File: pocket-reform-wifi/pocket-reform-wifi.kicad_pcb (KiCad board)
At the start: 4 copper layers, 27.6 x 95 mm, 42 parts, among them J1 Bus_M.2_Socket_E, J2 Conn_01x20, J21 CONN_HEAD, J22 SJ-43516-SMT, J24 CONN_PWRSW, SW21 SW_DIP_x01, U1 TPS62A04ABDRL, X1 ECS-327MVATX-2-CN-TR3

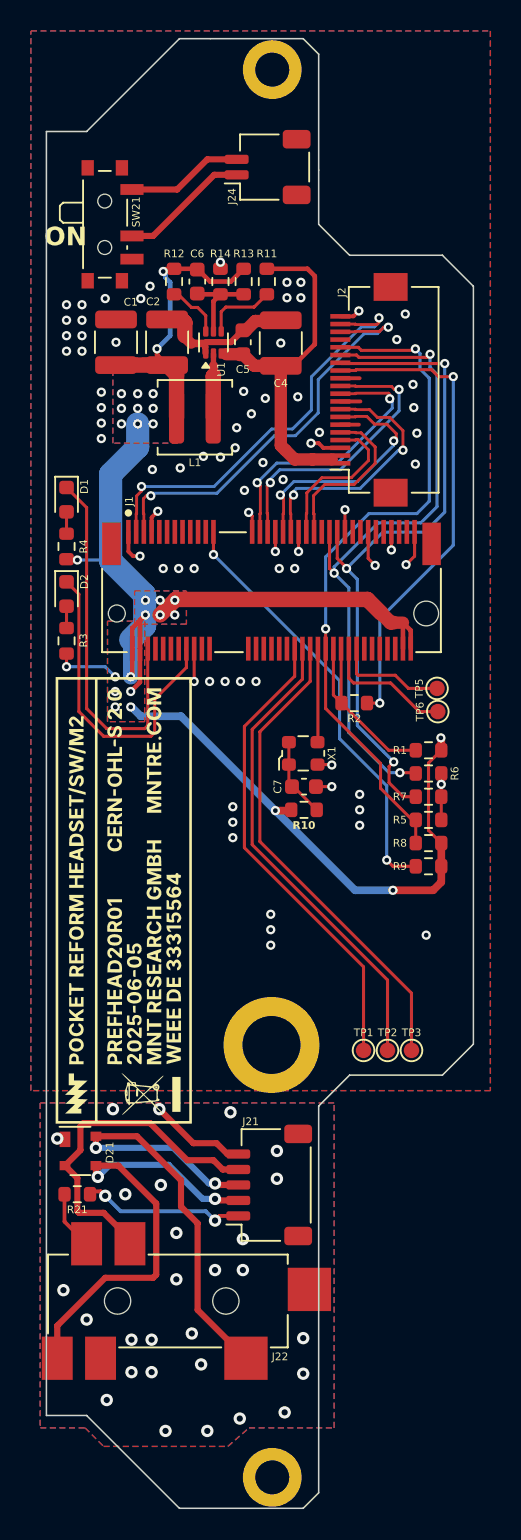
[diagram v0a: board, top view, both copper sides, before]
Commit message: pocket-reform-wifi: revision r2 with different inductor footprint
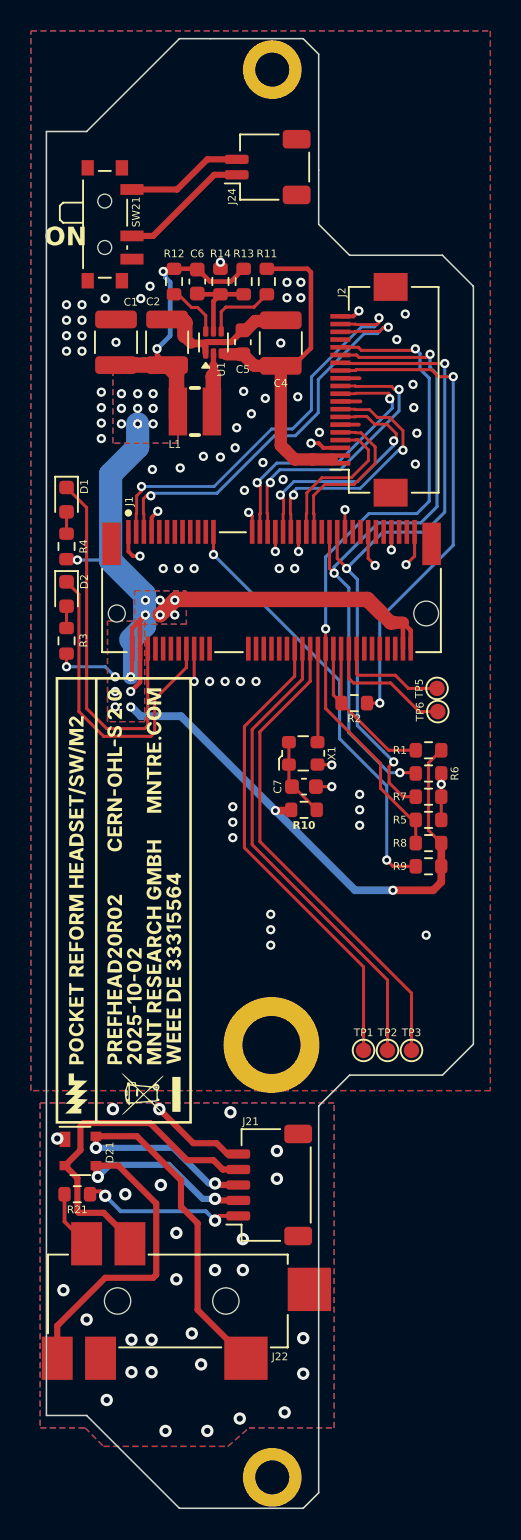
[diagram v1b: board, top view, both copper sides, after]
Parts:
- H1: footprint Mounting_Wuerth:Mounting_Wuerth_WA-SMSI-M2_H1.5mm_9774015243 -> footprints:Mounting_Sinhoo_SMTSO20
- L1: value 220nH XAL4020-221MEB -> 220nH 10A; footprint Inductor_SMD:L_Coilcraft_XAL4020-XXX -> EasyEDA:IND-SMD_L3.0-W3.0_FTC303020D
- moved L1 0.38 mm to (95.0, 101.1)
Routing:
- net +3V3: track 111.8 -> 111.0 mm, vias 28 -> 27

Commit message: pocket-reform-wifi: revision r2 part selection tweaks for new batch
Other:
- board text added: "JLCPCB Stackup JLC04101H-3313, 85 ohms diff impedance"
- board text removed: "JLCPCB Stackup JLC04081H-3313"
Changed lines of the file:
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@@
 			)
 		)
-		(property "Manufacturer_No" "2199119-4"
+		(property "Manufacturer_No" "2199230-4"
 			(at 0 0 0)
 			(unlocked yes)
@@
 			)
 		)
-		(property "Notes" ""
+		(property "Notes" "original was 2199119-4, 1mm less height. match with nut height!"
 			(at 0 0 0)
 			(unlocked yes)
@@
 			)
 		)
-		(property "Alt_Part_No" ""
+		(property "Alt_Part_No" "2199119-4 (with nut SMTSO2015CTJ)"
 			(at 0 0 0)
 			(unlocked yes)
@@
 			)
 		)
-		(property "LCSC" "global sourcing"
+		(property "LCSC" "C41447443"
 			(at 0 0 0)
 			(unlocked yes)
@@
 			)
 		)
-		(property "Manufacturer_No" "SMTSO2015CTJ"
+		(property "Manufacturer_No" "SMTSO2025CTJ"
 			(at 0 0 90)
 			(unlocked yes)
@@
 			)
 		)
-		(property "Notes" ""
+		(property "Notes" "match height with m.2 socket!"
 			(at 0 0 90)
 			(unlocked yes)
@@
 			)
 		)
-		(property "Alt_Manufacturer" "Wuerth"
+		(property "Alt_Manufacturer" ""
 			(at 0 0 90)
 			(unlocked yes)
@@
 			)
 		)
-		(property "Alt_Part_No" "9774015243"
+		(property "Alt_Part_No" "SMTSO2015CTJ for lower height m.2 socket"
 			(at 0 0 90)
 			(unlocked yes)
@@
 			)
 		)
-		(property "LCSC" "C2916320"
+		(property "LCSC" "C2916321"
 			(at 0 0 90)
 			(unlocked yes)
@@
 			)
 		)
-		(property "Manufacturer" "Vishay Dale"
+		(property "Manufacturer" "UNI-ROYAL"
 			(at 0 0 270)
 			(unlocked yes)
@@
 			)
 		)
-		(property "Manufacturer_No" "CRCW0603453KFKEA"
+		(property "Manufacturer_No" "0603WAF4533T5E"
 			(at 0 0 270)
 			(unlocked yes)
@@
 			)
 		)
-		(property "LCSC" "C2079749"
+		(property "LCSC" "C25818"
 			(at 0 0 270)
 			(unlocked yes)
@@
 			)
 		)
-		(property "Manufacturer" "ECS"
+		(property "Manufacturer" "SCTF"
 			(at 0 0 90)
 			(unlocked yes)
@@
 			)
 		)
-		(property "Manufacturer_No" "ECS-327MVATX-2-CN-TR3"
+		(property "Manufacturer_No" "SX2M32.768KM20F30TNN"
 			(at 0 0 90)
 			(unlocked yes)
@@
 			)
 		)
-		(property "LCSC" "C5375606"
+		(property "LCSC" "C2901603"
 			(at 0 0 90)
 			(unlocked yes)
@@
 		)
 	)
-	(gr_text "JLCPCB Stackup JLC04081H-3313"
+	(gr_text "JLCPCB Stackup JLC04101H-3313, 85 ohms diff impedance"
 		(at 82.4 84.1 270)
 		(layer "Cmts.User")
